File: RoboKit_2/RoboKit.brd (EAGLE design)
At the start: 134 x 82 mm, 28 parts, among them P1 B6B-PH-K, P2 B6B-PH-K, U1 CD74HC4067SM96, X1 JST-XH-03-PIN-LONG-PAD, X2 JST-XH-02-PIN-LONG-PAD, X3 JST-XH-02-PIN-LONG-PAD, X4 JST-XH-02-PIN-LONG-PAD, X5 JST-XH-04-PIN-LONG-PAD, X6 JST-XH-04-PIN-LONG-PAD, X7 JST-XH-10-PIN-LONG-PAD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

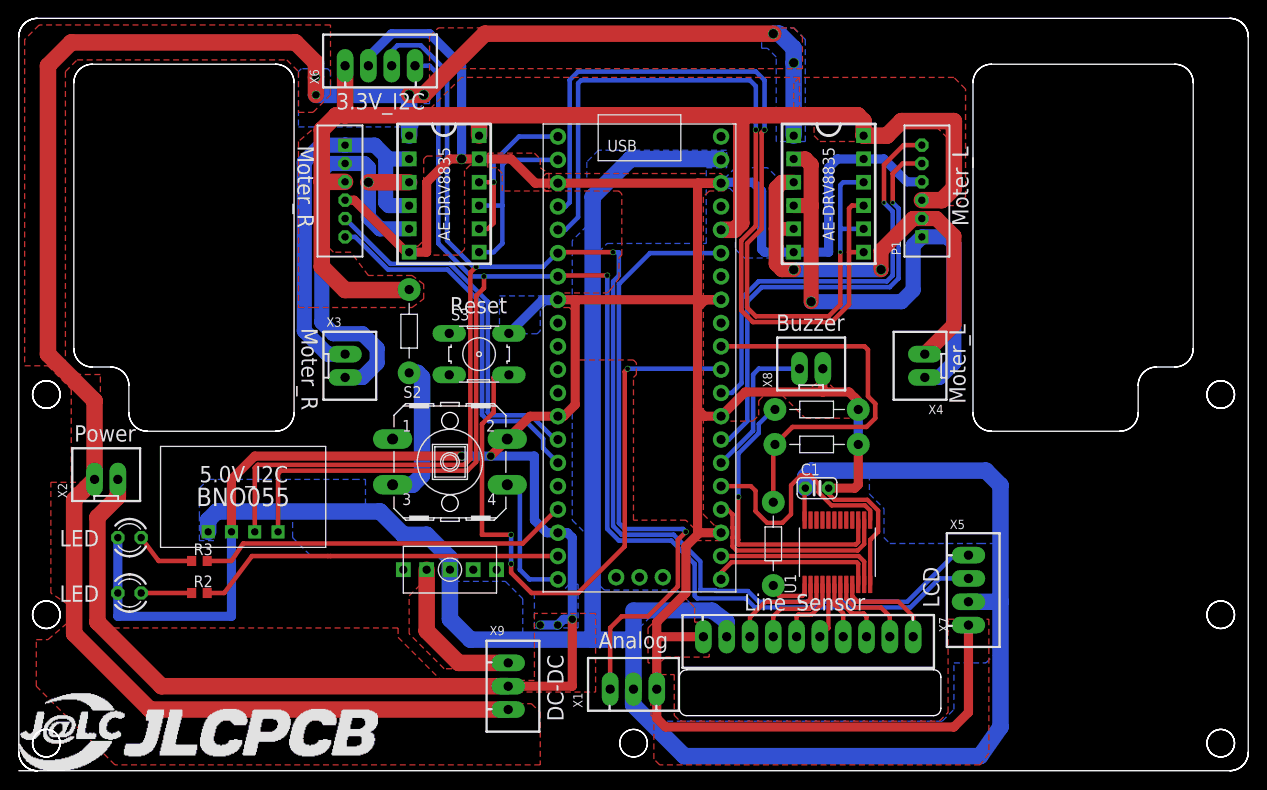
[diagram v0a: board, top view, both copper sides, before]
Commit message: XH10ピンが刺さらない不具合を修正し、アナログ出力の印刷が逆になっていたのを修正し、ver2.0のシルクを追加
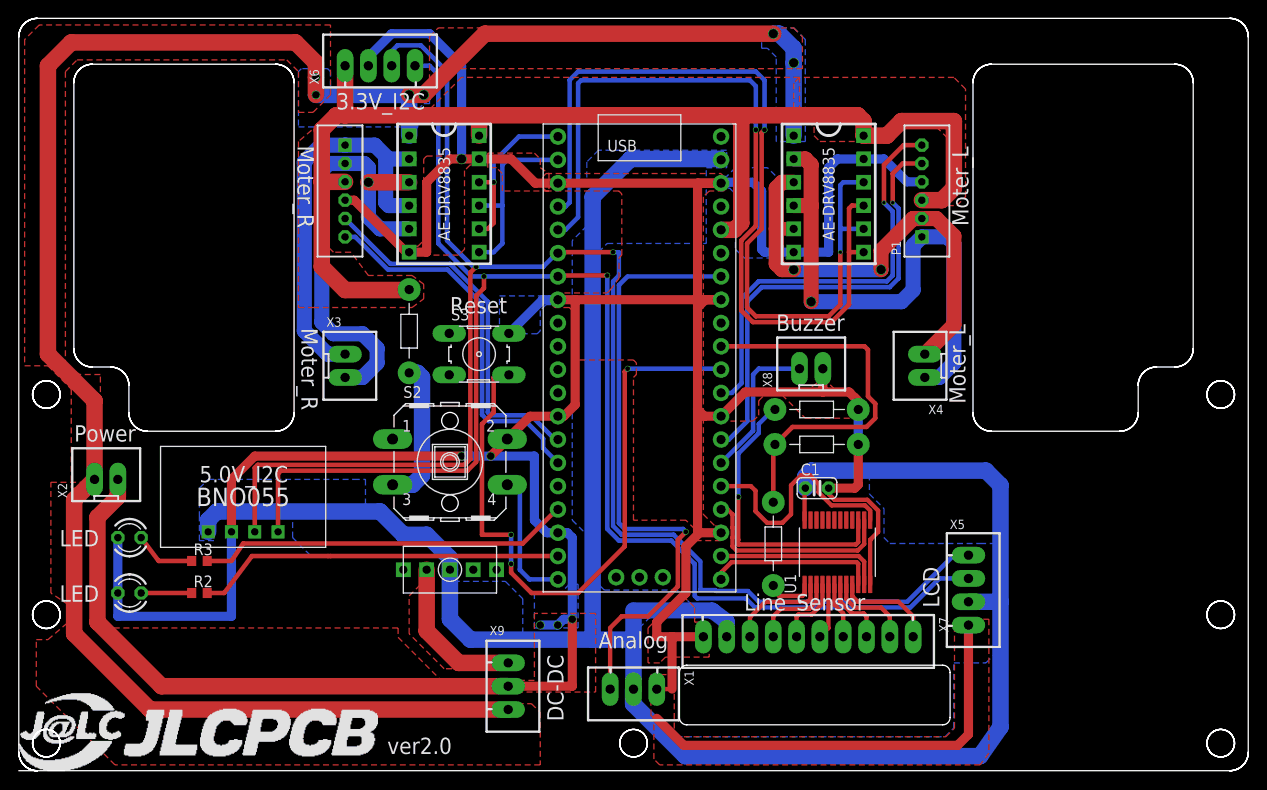
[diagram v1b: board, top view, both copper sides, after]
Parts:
- turned X1 to 180 degrees
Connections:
- removed net ADC2: U$1.34
- new net ADC_VREF: U$1.35
- net ANALOG: now also U$1.34, X1.3; no longer U$1.35, X1.1
- net GND: now also X1.1; no longer X1.3
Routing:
- net GND: track 504.8 -> 506.4 mm
- net ANALOG: track 68.5 -> 67.4 mm
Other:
- outline, holes or cut-outs redrawn
- board text added: "ver2.0"

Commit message: DRC通過
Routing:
- net GND: track 506.4 -> 458.8 mm
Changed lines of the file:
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@@
 <contactref element="X7" pad="10"/>
 <wire x1="74.6125" y1="13.97" x2="74.6125" y2="14.605" width="1" layer="1"/>
-<wire x1="72.485" y1="2.7625" x2="102.3175" y2="2.7625" width="1" layer="1"/>
-<wire x1="103.505" y1="3.95" x2="103.505" y2="15.875" width="1" layer="1"/>
-<wire x1="102.3175" y1="2.7625" x2="103.505" y2="3.95" width="1" layer="1"/>
 <wire x1="58.76" y1="25.935" x2="57.5675" y2="25.935" width="1" layer="16"/>
 <wire x1="56.1975" y1="27.305" x2="56.1975" y2="34.29" width="1" layer="16"/>
@@
 <wire x1="57.5675" y1="25.935" x2="56.1975" y2="27.305" width="1" layer="16"/>
 <wire x1="60.6425" y1="51.335" x2="76.54" y2="51.335" width="1" layer="1"/>
-<wire x1="69.5325" y1="5.715" x2="72.485" y2="2.7625" width="1" layer="1"/>
 <wire x1="74.6125" y1="14.605" x2="71.2" y2="14.605" width="1" layer="1"/>
 <polygon width="0.48" layer="1">
